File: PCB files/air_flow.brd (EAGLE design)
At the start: 100 x 80 mm, 66 parts, among them Q1 600mA/40V, U1 LM358, U2 LM358, U3 LMV358, U4 LMV358

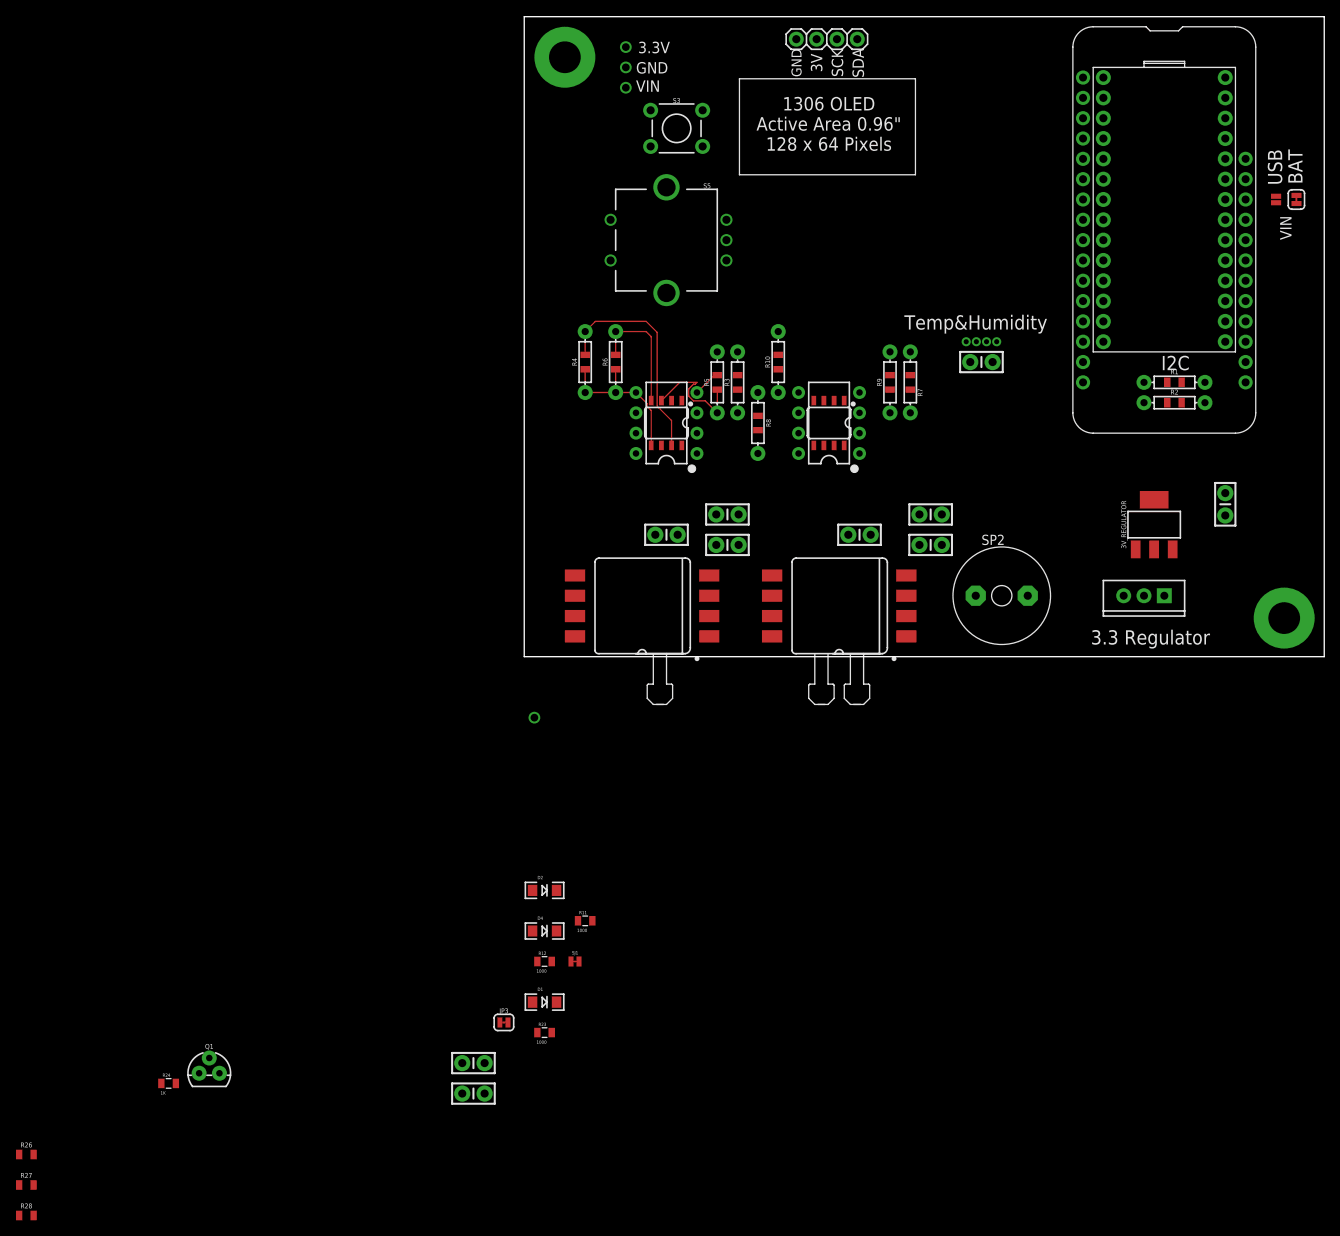
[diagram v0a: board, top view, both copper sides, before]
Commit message: updated ealge v0 to JLCPCB
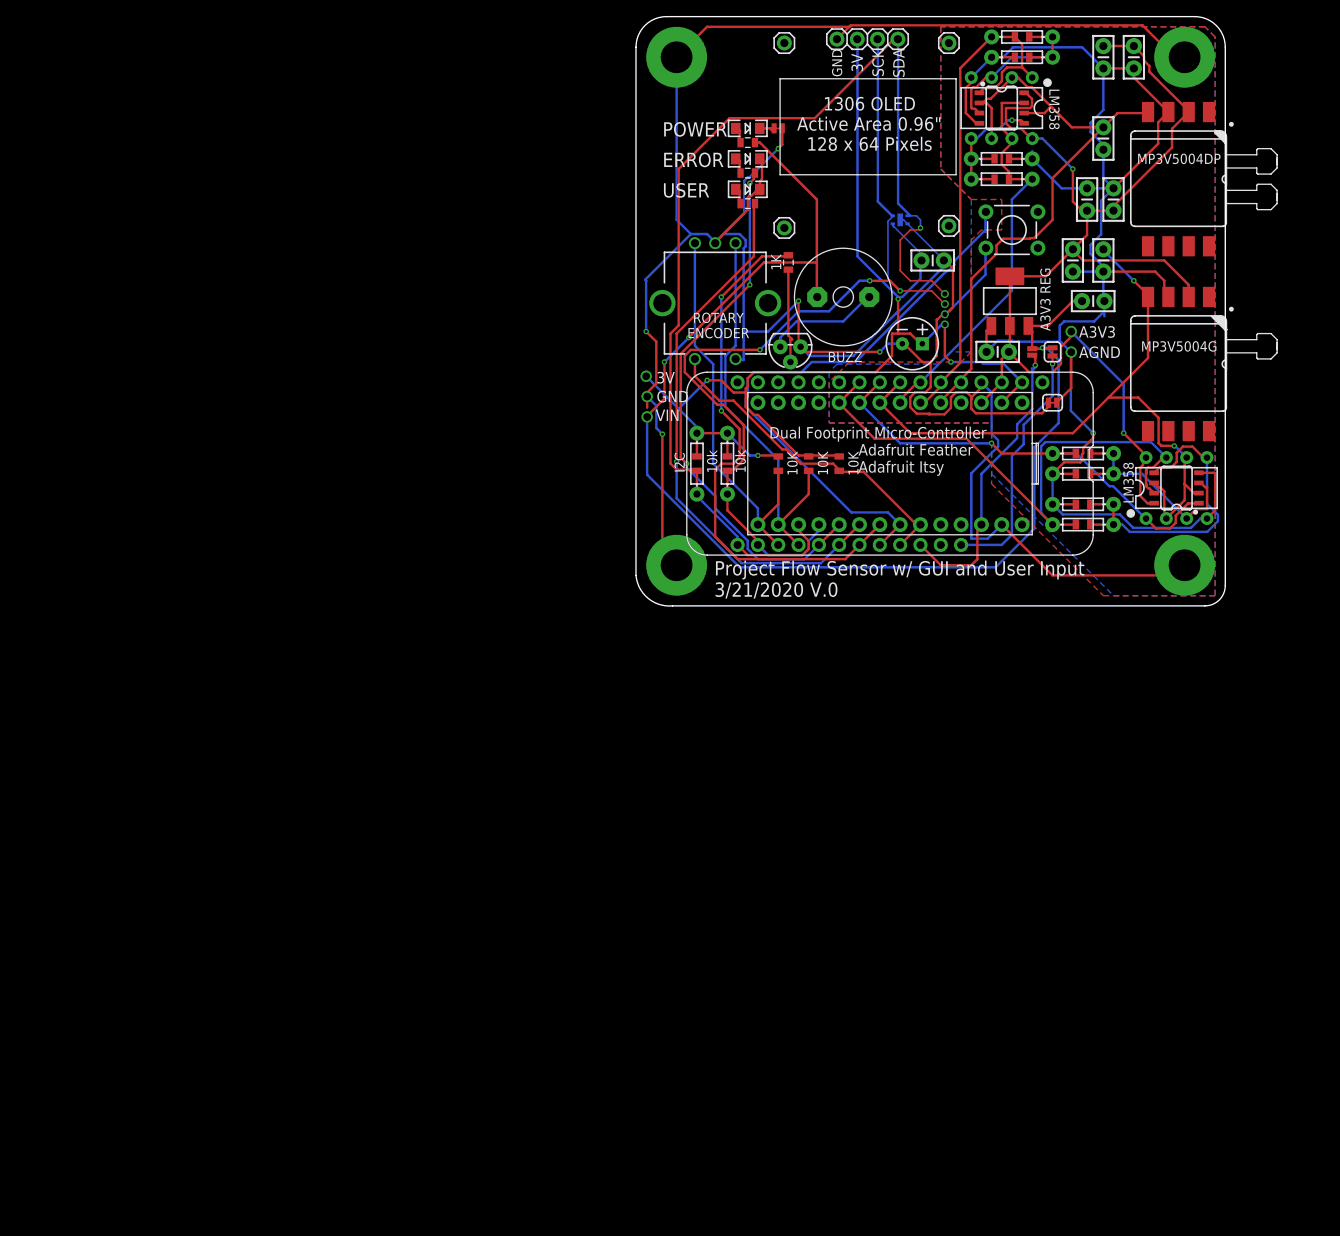
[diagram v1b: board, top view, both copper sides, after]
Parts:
- removed Q1: 600mA/40V, SparkFun-DiscreteSemi:TO-92
- removed U7: (no value), SparkFun-IC-Power:TO220-IGO
- added C11: 100uF, SparkFun-Capacitors:CPOL-RADIAL-2.5MM-6.5MM
- added J1, J2, J3, J4: (no value), SparkFun-Connectors:1X01
- added Q2: 200mA/40V, SparkFun-DiscreteSemi:TO-92
- added S4, S6: STANDOFF_ELECTRICAL5-32, th_libraries:STANDOFF_ELECTRICAL_5_32
- added U$26: CONN_0138MILL, th_libraries3:1X01-40MILL
- added U5: SHTC3, SHTC3:SHTC3
- moved R28 138.4 mm to (39.4, 24.1), turned to 90 degrees
- moved R27 133.0 mm to (35.6, 24.1), turned to 270 degrees
- moved R24 128.6 mm to (33.0, 49.3), turned to 90 degrees
- moved C8 128.3 mm to (68.6, 49.5), turned to 270 degrees
- moved R26 127.6 mm to (31.8, 24.1), turned to 90 degrees
- moved C10 110.4 mm to (59.2, 38.1)
- moved R23 110.4 mm to (27.9, 60.5)
- moved D1 108.4 mm to (27.9, 62.2)
- moved SJ1 107.2 mm to (31.8, 66.0), turned to 180 degrees
- moved R12 105.5 mm to (27.9, 64.3)
- moved JP3 103.5 mm to (66.0, 31.8), turned to 180 degrees
- moved D2 98.6 mm to (27.9, 66.0)
- moved D4 96.1 mm to (27.9, 58.4)
- moved R11 91.9 mm to (27.9, 56.6)
- moved S2 76.2 mm to (19.1, 11.4)
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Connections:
- removed net A0: MS2.5
- removed net A3: MS2.8
- new net N$13: MS2.15
- new net N$14: MS2.14
- new net N$15: MS2.13
- new net N$16: MS2.12
- new net N$17: MS2.11
- new net N$7: MS2.16
- net 3.3V: now also MS2.3; no longer U7.OUT
- net 3V: now also C11.1, MS2.2, U5.1
- net A4: now also MS2.9
- net A5: now also MS2.10
- net AGND: now also U$26.1; no longer U7.GND
- net D_OUT: now also MS2.5
- net GND: now also C11.2, Q2.1, S4.P1, S6.P1, U5.4, U5.5; no longer Q1.3
- net LED_ERROR: now also MS2.22
- net LED_TBD: now also MS2.21
- net N$10: now also Q2.2; no longer Q1.2
- net N$9: now also Q2.3; no longer Q1.1
- net PWM_BUZZER: now also MS2.23
- net ROTARY_A: now also MS2.20
- net ROTARY_B: now also MS2.19
- net ROTARY_SWITCH: now also MS2.25
- net SCL: now also U5.2
- net SDA: now also U5.3
- net SWITCH1: now also MS2.24
- net S_OUT: now also MS2.8
- net VIN: no longer U7.IN
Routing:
- net GND: track 0.00 -> 367.9 mm, vias 0 -> 5
- net AGND: track 19.1 -> 206.2 mm, vias 0 -> 1
- net VIN: track 0.00 -> 156.0 mm, vias 0 -> 3
- net 3V: track 0.00 -> 155.5 mm, vias 0 -> 4
- net 3.3V: track 0.00 -> 148.6 mm, vias 0 -> 2
- net SDA: track 0.00 -> 139.3 mm, vias 0 -> 1
- net SCL: track 0.00 -> 111.5 mm, vias 0 -> 3
- net S_OUT: track 0.00 -> 89.4 mm, vias 0 -> 2
- net D_OUT: track 0.00 -> 80.4 mm
- net SWITCH1: track 0.00 -> 72.9 mm
- net LED_ERROR: track 0.00 -> 69.2 mm, vias 0 -> 1
- net LED_TBD: track 0.00 -> 68.1 mm, vias 0 -> 3
- net PWM_BUZZER: track 0.00 -> 67.2 mm, vias 0 -> 2
- net A1: track 0.00 -> 65.9 mm
- net A4: track 0.00 -> 57.3 mm, vias 0 -> 1
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- added copper zone on layer 1, net AGND
- added copper zone on layer 16, net AGND
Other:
- board size 100 x 80 mm -> 73.7 x 73.7 mm
- board text added: "2"
- board text added: "3V"
- board text added: "A1"
- board text added: "A2"
- board text added: "A3V3"
- board text added: "A3V3 REG"
- board text added: "A4"
- board text added: "A5"
- board text added: "AGND"
- board text added: "AREF"
- board text added: "BUZZ"
- board text added: "D12"
- board text added: "D13"
- board text added: "D_O"
- board text added: "D_OUT"
- board text added: "Dual Footprint Micro-Controller Adafruit Feather Adafruit Itsy"
- board text added: "ENCOD_A"
- board text added: "ENCOD_B"
- board text added: "ENCO_A"
- board text added: "ENCO_B"
- board text added: "ERROR"
- board text added: "HIH8120"
- board text added: "LED_E"
- board text added: "LED_TB"
- board text added: "LM358"
- board text added: "MISO"
- board text added: "MOSI"
- board text added: "MP3V5004DP"
- board text added: "MP3V5004G"
- board text added: "POWER"
- board text added: "Project Flow Sensor w/ GUI and User Input 3/21/2020 V.0"
- board text added: "ROTARY ENCODER"
- board text added: "R_SW"
- board text added: "SCK"
- board text added: "SCL"
- board text added: "SDA"
- board text added: "SHTC3"
- board text added: "S_O"
- board text added: "S_OUT"
- board text added: "USER"
- board text added: "U_SW"
- board text added: "VBAT"
- board text removed: "3.3 Regulator"
- board text removed: "3.3V"
- board text removed: "BAT"
- board text removed: "Temp&Humidity"
